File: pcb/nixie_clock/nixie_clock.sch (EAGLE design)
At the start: 38 parts, among them Q1 IRLR3110ZPBF, T1 DA2032-AL, U1 ESP32, U2 CP2102N, U3 LT3757

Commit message: sch and pcb outline
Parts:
- added C12: 0.22F, Passive Components > Capacitors > Supercapacitors \ Ultracapacitors:DSK-614/621
- added C13, C14, C18, C19: 1u, Passive Components > Capacitors > Multilayer Ceramic Capacitors MLCC:MLCC0603
- added C15: 22n, Passive Components > Capacitors > Multilayer Ceramic Capacitors MLCC:MLCC0603
- added C16, C17, C20, C23, C26, C27, C28, C29, C30, C31, C40: 100n, Passive Components > Capacitors > Multilayer Ceramic Capacitors MLCC:MLCC0603
- added C21: 4u7, Passive Components > Capacitors > Multilayer Ceramic Capacitors MLCC:MLCC0603
- added C22: 100p, Passive Components > Capacitors > Multilayer Ceramic Capacitors MLCC:MLCC0603
- added C24, C25: 15p, Passive Components > Capacitors > Multilayer Ceramic Capacitors MLCC:MLCC0603
- added C32: 10n, Passive Components > Capacitors > Multilayer Ceramic Capacitors MLCC:MLCC0603
- added C33: 3n, Passive Components > Capacitors > Multilayer Ceramic Capacitors MLCC:MLCC0603
- added C34, C35: 270p, Passive Components > Capacitors > Multilayer Ceramic Capacitors MLCC:MLCC0603
- added C36, C37: 10p, Passive Components > Capacitors > Multilayer Ceramic Capacitors MLCC:MLCC0603
- added C38: 5p6, Passive Components > Capacitors > Multilayer Ceramic Capacitors MLCC:MLCC0603
- added C39: 2p4, Passive Components > Capacitors > Multilayer Ceramic Capacitors MLCC:MLCC0603
- added D6: B0530W, Semiconductors > Discrete Semiconductors > Diodes & Rectifiers > Schottky Diodes & Rectifiers:B0530W
- added D7, D8: LED0603, Opto-electronics > LED Emitters:LED0603
- added F1: (no value), Circuit Protection > Resettable Fuses - PPTC:PTC0805
- added J1: USB-C, Connectors > USB:USB-C
- added L1: 10u, Passive Components > Inductors, Chokes & Coils:INDUCTOR_NC_1210
- added L2: 2n7, Passive Components > Inductors, Chokes & Coils:INDUCTOR_NC_0603
- added NL1, NL2: NEON6X16, vacuum_tubes:NEON6X16
- added Q2, Q3, Q4, Q5, Q6, Q7: BC817-25, Semiconductors > Discrete Semiconductors > Transistors > Bipolar Transistors - BJT:BC817-25
- added R13: 94k, Passive Components > Resistors > Chip Resistors:RESISTOR0603
- added R14, R16, R25, R33, R34, R35: 10k, Passive Components > Resistors > Chip Resistors:RESISTOR0603
- added R15: 85k, Passive Components > Resistors > Chip Resistors:RESISTOR0603
- added R17, R18: 100k, Passive Components > Resistors > Chip Resistors:RESISTOR_1206
- added R23, R24, R28, R29: 11k5, Passive Components > Resistors > Chip Resistors:RESISTOR0603
- added R26: 47k5, Passive Components > Resistors > Chip Resistors:RESISTOR0603
- added R27: 22k1, Passive Components > Resistors > Chip Resistors:RESISTOR0603
- added R30, R31, R38: 1k, Passive Components > Resistors > Chip Resistors:RESISTOR0603
- added R32: 20k, Passive Components > Resistors > Chip Resistors:RESISTOR0603
- added R36, R37: 4k7, Passive Components > Resistors > Chip Resistors:RESISTOR0603
- added SW1, SW2: (no value), Eletromechanical > Switches > Tactile Switches:PUSH_BUTTON
- added U$1: MIC2619, Power > Switching Controllers:MIC2619
- added U4: DS3231, Semiconductors > Integrated Circuits - ICs > Clock & Timer ICs > Real Time Clock:DS3231
- added U5, U6: HV5522, Power > Power Switch:HV5522
- added U7: MCP1700T-3302TT, Power > LDO Voltage Regulators:MCP1700T-3302TT
- added U8: W25Q40BVSS, Semiconductors > Integrated Circuits - ICs > Memory ICs > Flash:W25Q40BVSS
- added X1: 32.768kHz, Passive Components > Frequency Control & Timing Devices > Crystals:CRYSTAL2-SMD-3215
- added X2: 26MHz, Passive Components > Frequency Control & Timing Devices > Crystals:CRYSTAL_4P
- R10, R11, R12, R9: value (none) -> 15k
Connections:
- new net !DSP_BL: U1.(DAC1/ADC2:8/RTC6)GPIO25
- new net !DSP_LE: U1.(GPIO15/ADC2:3/TOUCH3/RTC13/SPICSO/U0RTS)MTDO
- new net 12V: C14.P$1, C15.P$1, C16.P$1, C17.P$1, D6.C, R13.P$2, R15.P$2, U5.!POL, U5.VDD, U6.!POL, U6.VDD
- new net 3.3V: C19.P$1, C20.P$1, C21.P$1, C22.P$1, C23.P$1, C26.P$1, C27.P$1, C28.P$1, C30.P$1, C31.P$1, C40.P$1, R25.P$2, R28.P$2, R29.P$2, R35.P$2, R36.P$2, R37.P$2, R38.P$2, U1.VDD3P3_CPU, U1.VDD3P3_RTC, U1.VDDA, U1.VDDA3P3, U2.VDD@6, U2.VIO@5, U2.VREGIN@7, U4.VCC, U7.VO, U8.VCC
- new net CHIP_PU: Q3.C03, R28.P$1, SW1.LB, SW1.RB, U1.CHIP_PU
- new net DSP_BL_CLK: D2.CLKI@4, U1.(VSPICLK/HS1_DATA7)GPIO18
- new net DSP_BL_SDI: D2.SDI@3, U1.GPIO23
- new net DSP_CLK: U1.(GPIO14/ADC2:6/TOUCH6/RTC16/SPICLK)MTMS
- new net DSP_SDI: U1.(GPIO13/ADC2:4/TOUCH4/RTC14/SPID/U0CTS)MTCK
- new net DTR: Q2.EM2, R34.P$2, U2.DTR@23
- new net FLASH_SCK: U1.(GPIO6/SPICLK/HS1_CLK/U1CTS)SD_CLK, U8.CLK
- new net FLASH_SCS: U1.(GPIO11/SPICSO/HS1_CMD/U1RTS)SD_CMD, U8.!CS!
- new net FLASH_SDI: U1.(GPIO8/SPID/HS1_DATA1)SD_DATA1, U8.DI/IO0
- new net FLASH_SDO: U1.(GPIO7/SPI1/HS1_DATA0)SD_DATA0, U8.DO/IO1
- new net FLASH_SHD: U1.(GPIO9/SPIHD/HS1_DATA2/U1RX)SD_DATA2, U8.!HOLD!/IO3
- new net FLASH_SWP: U1.(GPIO10/SPIWP/HS1_DATA3/U1TX)SD_DATA3, U8.!WP!/IO2
- new net FLASH_VDD: C29.P$1, U1.VDD3P3_SDIO
- new net GPIO0-BOOT: Q2.C03, R29.P$1, SW2.LB, SW2.RB, U1.(ADC2:1/TOUCH1/RTC11/CLK_OUT1)GPIO0
- new net HFXTAL_N: C36.P$1, U1.XTAL_N, X2.1
- new net HFXTAL_P: C37.P$1, U1.XTAL_P, X2.2
- new net LED: D7.AN, U1.(VSPICS0/HS1_DATA6)GPIO5
- new net LFXTAL_N: C25.P$1, U1.32K_XN(GPIO33/ADC1:5/TOUCH8/RTC8), X1.2
- new net LFXTAL_P: C24.P$1, U1.32K_XP(GPIO32/ADC1:4/TOUCH9/RTC9), X1.1
- new net N$16: D6.A, L1.P$2, U$1.SW
- new net N$17: R13.P$1, R14.P$2, U$1.OVP
- new net N$18: C15.P$2, R15.P$1, R16.P$2, U$1.FB
- new net N$19: NL1.2, R17.P$1
- new net N$20: NL2.2, R18.P$1
- new net N$23: U5.SDO, U6.SDI
- new net N$72: D3.SDO@1, D4.SDI@3
- new net N$73: D3.CLKO@6, D4.CLKI@4
- new net N$74: F1.2, J1.VBUS@A4,A9,B9,B4
- new net N$75: J1.CC2@B5, R23.P$2
- new net N$76: D4.CLKO@6, D5.CLKI@4
- new net N$77: D4.SDO@1, D5.SDI@3
- new net N$78: J1.CC1@A5, R24.P$2
- new net N$79: R25.P$1, U2.RSTB@9
- new net N$80: D8.CA, R30.P$2
- new net N$81: D2.CLKO@6, D3.CLKI@4
- new net N$82: D2.SDO@1, D3.SDI@3
- new net N$83: R26.P$2, R27.P$1, U2.VBUS@8
- new net N$84: D7.CA, R31.P$2
- new net N$85: C33.P$1, R32.P$2, U1.CAP2
- new net N$86: C34.P$1, U1.SENSOR_VN(GPI39/ADC1:3/RTC3)
- new net N$87: C32.P$1, C33.P$2, R32.P$1, U1.CAP1
- new net N$88: C35.P$1, U1.SENSOR_VP(GPI36/ADC1:0/RTC0)
- new net N$89: C34.P$2, U1.SENSOR_CAPN(GPI38/ADC1:2/RTC2)
- new net N$90: C35.P$2, U1.SENSOR_CAPP(GPI37/ADC1:1/RTC1)
- new net N$91: C38.P$1, L2.P$2, U1.LNA_IN
- new net N$92: Q2.BA1, R33.P$1
- new net N$93: Q3.BA1, R34.P$1
- new net N$94: C38.P$2, C39.P$1, E1.SIGNAL
- new net N$95: C12.AN, U4.VBAT
- new net N$96: R35.P$1, U4.!RST
- new net NT1-0: NT1.0, U5.HVOUT11
- new net NT1-1: NT1.1, U5.HVOUT12
- new net NT1-2: NT1.2, U5.HVOUT13
- new net NT1-3: NT1.3, U5.HVOUT14
- new net NT1-4: NT1.4, U5.HVOUT15
- new net NT1-5: NT1.5, U5.HVOUT16
- new net NT1-6: NT1.6, U5.HVOUT17
- new net NT1-7: NT1.7, U5.HVOUT18
- new net NT1-8: NT1.8, U5.HVOUT19
- new net NT1-9: NT1.9, U5.HVOUT20
- new net NT2-0: NT2.0, U5.HVOUT1
- new net NT2-1: NT2.1, U5.HVOUT2
- new net NT2-2: NT2.2, U5.HVOUT3
- new net NT2-3: NT2.3, U5.HVOUT4
- new net NT2-4: NT2.4, U5.HVOUT5
- new net NT2-5: NT2.5, U5.HVOUT6
- new net NT2-6: NT2.6, U5.HVOUT7
- new net NT2-7: NT2.7, U5.HVOUT8
- new net NT2-8: NT2.8, U5.HVOUT9
- new net NT2-9: NT2.9, U5.HVOUT10
- new net RTC_INT: R38.P$1, U1.(ADC2:0/TOUCH0/RTC10/SPIHD)GPIO4, U4.!INT!/SQW
- new net RTS: Q3.EM2, R33.P$2, U2.RTS@19
- new net SCL: R37.P$1, U1.(VSPIWP/HS2_CLK)GPIO22, U4.SCL
- new net SDA: R36.P$1, U1.(VSPIHD/HS2_CMD)GPIO21, U4.SDA
- new net U0RXD: U1.(GPIO3/CLK_OUT2/HS2_DATA0)U0RXD, U2.TXD@21
- new net U0TXD: U1.(GPIO1/CLK_OUT3/HS2_DATA1)U0TXD, U2.RXD@20
- new net USB_DM: J1.DN@A7,B7, U2.D-@4
- new net USB_DP: J1.DP@A6,B6, U2.D+@3
- net !HVEN: now also U1.(DAC2/ADC2:9/RTC7)GPIO26
- net 5V: now also C13.P$1, C18.P$1, D2.VDD@5, D3.VDD@5, D4.VDD@5, D5.VDD@5, D8.AN, F1.1, L1.P$1, R27.P$2, U$1.EN, U$1.VIN, U7.VI
- net GND: now also C12.CA, C13.P$2, C14.P$2, C16.P$2, C17.P$2, C18.P$2, C19.P$2, C20.P$2, C21.P$2, C22.P$2, C23.P$2, C24.P$2, C25.P$2, C26.P$2, C27.P$2, C28.P$2, C29.P$2, C30.P$2, C31.P$2, C32.P$2, C36.P$2, C37.P$2, C39.P$2, C40.P$2, D2.GND@2, D3.GND@2, D4.GND@2, D5.GND@2, E1.GND, J1.GND@A1,A12,B12,B1, J1.SHIELD, L2.P$1, R14.P$1, R16.P$1, R23.P$1, R24.P$1, R26.P$1, R30.P$1, R31.P$1, SW1.LT, SW1.RT, SW2.LT, SW2.RT, U$1.GND, U1.GND, U2.GND@2, U2.GND@PAD, U4.GND, U4.NC, U5.GND, U6.GND, U7.GND, U8.GND, X2.GND@0, X2.GND@1
- net VOUT: now also R17.P$2, R18.P$2
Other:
- note added: "32.768kHz RTC Crystal"
- note added: "Auto-Reset"
- note added: "Boot Mode Configuration Pin Default Boot Download GPIO0 1 1 0 U0TXD 1 1 x GPIO2 0 x 0 GPIO4 0 x x MTDO 1 x x GPIO5 1 1 x If U0TXD, GPIO2, GPIO5 are floating, GPIO0 determines boot mode"
- note added: "CHIP_PU is the ESP32's enable/reset pin. It must be pulled high to turn the ESP32 on."
- note added: "CP2102N (USB-to-Serial Converter)"
- note added: "DS3231 RTCC"
- note added: "Espressif ESP32"
- note added: "GPIO0 Button"
- note added: "GPIO5 LED"
- note added: "Headers"
- note added: "If DTR is LOW, toggling RTS from HIGH to LOW resets to run mode. If RTS is HIGH, toggling DTR from LOW to HIGH resets to bootloader."
- note added: "Near VDDA 46, 43"
- note added: "Near VDDA3P3 3, 4"
- note added: "Near VDDA_LNA 1"
- note added: "Near VDDPST_CPU 37"
- note added: "Near VDDPST_RTC 19"
- note added: "Near VDDPST_SDIO 26"
- note added: "R13: 10k R14: 85K Vo: 12.017 V"
- note added: "R13: 10k R14: 94k OVP: 13.156 V"
- note added: "Reset Button"
- note added: "SJ3 allows selection between FLASH_VDD and 3.3V as the voltage supply to the flash IC."
- note added: "Vfb = 1.265 V"
- note added: "Voltage Regulator and input connector"
- note added: "W25Q32FVSS - 4MB SPI Flash"
- moved on the sheet: D2, D3, D4, D5, E1, NT1, NT2, NT3, NT4, R10, R11, R12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

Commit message: rough pcb done
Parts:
- removed U$1: MIC2619, Power > Switching Controllers:MIC2619
- added C41, C42, C43, C44: (no value), Passive Components > Capacitors > Multilayer Ceramic Capacitors MLCC:MLCC0603
- added C45: 47u, Passive Components > Capacitors > Multilayer Ceramic Capacitors MLCC:MLCC_1210
- added D9: BAT54S, Semiconductors > Discrete Semiconductors > Diodes & Rectifiers > Schottky Diodes & Rectifiers:BAT54S
- added J2, J3: 8, Connectors > Header:8
- added J4, J5: 4, Connectors > Header:4
- added LOGO1, LOGO8: DESIGNEDINPT, Utility > Silkscreen:DESIGNEDINPT
- added LOGO2: RAFAEL_SILVA10CIRCLE, Utility > Silkscreen:RAFAEL_SILVA10CIRCLE
- added LOGO3, LOGO9: OSHW-LOGOL, Utility > Silkscreen:OSHW-LOGOL
- added LOGO4, LOGO6: HV_WARNING, Silkscreen:HV_WARNING
- added LOGO5: RADIO-10MM, Silkscreen:RADIO-10MM
- added LOGO7: RAFAEL_SILVA10MM, Utility > Silkscreen:RAFAEL_SILVA10MM
- added R19, R21, R22, R39, R40, R41, R42: 1k, Passive Components > Resistors > Chip Resistors:RESISTOR0603
- added R20: 94k, Passive Components > Resistors > Chip Resistors:RESISTOR0603
- added R43: 100, Passive Components > Resistors > Chip Resistors:RESISTOR0603
- added R44: 10k, Passive Components > Resistors > Chip Resistors:RESISTOR0603
- added U10, U11: 74LVC1G17, Semiconductors > Integrated Circuits - ICs > Logic ICs > Logic Gates:74LVC1G17
- added U9: MIC2619, Power > Switching Controllers:MIC2619
- C33: value 3n -> 3n3
- E1: value ANTENNATRACE-15.2MM -> ANTENNATRACE; device Passive Components > Antennas:ANTENNATRACE-15.2MM -> Passive Components > Antennas:ANTENNATRACE
- R6: value 10k -> 100k
- R7: value 75k -> 10k
- SW1, SW2: device Eletromechanical > Switches > Tactile Switches:PUSH_BUTTON -> Eletromechanical > Switches > Tactile Switches:PUSH_BUTTON3X4X2
- U7: value MCP1700T-3302TT -> MIC39100; device Power > LDO Voltage Regulators:MCP1700T-3302TT -> Power > LDO Voltage Regulators:MIC39100
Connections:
- removed net N$94: C38.P$2, C39.P$1, E1.SIGNAL
- new net !DSP_BL_HL: J2-7.S, Q7.C03, R42.P$1
- new net !DSP_LE_HL: J2-6.S, Q6.C03, R41.P$1
- new net BR2_DSP_CLK_HL: J3-5.S, U5.CLK, U6.CLK
- new net BRD2_!DSP_BL_HL: J3-7.S, U5.!BL, U6.!BL
- new net BRD2_!DSP_LE_HL: J3-6.S, U5.!LE, U6.!LE
- new net BRD2_12V: C16.P$1, C17.P$1, J3-3.S, U5.!POL, U5.VDD, U6.!POL, U6.VDD
- new net BRD2_GND2: C16.P$2, C17.P$2, J3-8.S, U5.GND, U6.GND
- new net BRD2_SDP_SDI_HL: J3-4.S, U5.SDI
- new net BRD2_VOUT: J3-1.S, R10.P$2, R11.P$2, R12.P$2, R17.P$2, R18.P$2, R9.P$2
- new net DSP_CLK_HL: J2-5.S, Q5.C03, R40.P$1
- new net LED_GND: C41.P$2, C42.P$2, C43.P$2, C44.P$2, D2.GND@2, D3.GND@2, D4.GND@2, D5.GND@2, J5-2.S
- new net LED_VCC: C41.P$1, C42.P$1, C43.P$1, C44.P$1, D2.VDD@5, D3.VDD@5, D4.VDD@5, D5.VDD@5, J5-3.S
- new net N$21: Q4.BA1, R19.P$2
- new net N$22: Q5.BA1, R20.P$2
- new net N$24: Q7.BA1, R22.P$2
- new net N$25: Q6.BA1, R21.P$2
- new net N$26: D2.SDI@3, J5-1.S
- new net N$27: D2.CLKI@4, J5-4.S
- new net N$28: C39.P$1, E1.SIGNAL, L2.P$1
- new net N$29: J4-4.S, U11.1.Y
- new net N$30: J4-1.S, U10.1.Y
- new net N$31: D9.3, R43.P$2
- new net N$32: R44.P$2, R6.3, U3.FB
- new net NL1: NL1.2, U6.HVOUT21
- new net NL2: NL2.2, U6.HVOUT22
- new net NT3-0: NT3.0, U6.HVOUT11
- new net NT3-1: NT3.1, U6.HVOUT12
- new net NT3-2: NT3.2, U6.HVOUT13
- new net NT3-3: NT3.3, U6.HVOUT14
- new net NT3-4: NT3.4, U6.HVOUT15
- new net NT3-5: NT3.5, U6.HVOUT16
- new net NT3-6: NT3.6, U6.HVOUT17
- new net NT3-7: NT3.7, U6.HVOUT18
- new net NT3-8: NT3.8, U6.HVOUT19
- new net NT3-9: NT3.9, U6.HVOUT20
- new net NT4-0: NT4.0, U6.HVOUT1
- new net NT4-1: NT4.1, U6.HVOUT2
- new net NT4-2: NT4.2, U6.HVOUT3
- new net NT4-3: NT4.3, U6.HVOUT4
- new net NT4-4: NT4.4, U6.HVOUT5
- new net NT4-5: NT4.5, U6.HVOUT6
- new net NT4-6: NT4.6, U6.HVOUT7
- new net NT4-7: NT4.7, U6.HVOUT8
- new net NT4-8: NT4.8, U6.HVOUT9
- new net NT4-9: NT4.9, U6.HVOUT10
- new net SDP_SDI_HL: J2-4.S, Q4.C03, R39.P$1
- net !DSP_BL: now also R22.P$1
- net !DSP_LE: now also R21.P$1
- net 12V: now also J2-3.S, R39.P$2, R40.P$2, R41.P$2, R42.P$2; no longer C16.P$1, C17.P$1, U5.!POL, U5.VDD, U6.!POL, U6.VDD
- net 3.3V: now also D9.1, U7.VOUT; no longer U7.VO
- net 5V: now also C45.P$1, J4-3.S, U10.PW.VCC, U11.PW.VCC, U7.VIN, U9.EN, U9.VIN; no longer D2.VDD@5, D3.VDD@5, D4.VDD@5, D5.VDD@5, U$1.EN, U$1.VIN, U7.VI
- net CHIP_PU: now also SW1.4; no longer SW1.LB, SW1.RB
- net DSP_BL_CLK: now also U11.1.A; no longer D2.CLKI@4
- net DSP_BL_SDI: now also U10.1.A; no longer D2.SDI@3
- net DSP_CLK: now also R20.P$1
- net DSP_SDI: now also R19.P$1
- net GND: now also C38.P$2, C45.P$2, J2-8.S, J4-2.S, Q4.EM2, Q5.EM2, Q6.EM2, Q7.EM2, R44.P$1, SW1.1, SW1.2, SW2.1, SW2.2, T1.1, U10.PW.GND, U11.PW.GND, U7.GND_(TAB), U7.GND_(TAB)_2, U9.GND; no longer C16.P$2, C17.P$2, D2.GND@2, D3.GND@2, D4.GND@2, D5.GND@2, L2.P$1, R6.2, SW1.LT, SW1.RT, SW2.LT, SW2.RT, U$1.GND, U5.GND, U6.GND, U7.GND
- net GPIO0-BOOT: now also SW2.4; no longer SW2.LB, SW2.RB
- net HFXTAL_N: now also C37.P$1, X2.2; no longer C36.P$1, X2.1
- net HFXTAL_P: now also C36.P$1, X2.1; no longer C37.P$1, X2.2
- net N$16: now also U9.SW; no longer U$1.SW
- net N$17: now also U9.OVP; no longer U$1.OVP
- net N$18: now also U9.FB; no longer U$1.FB
- net N$19: now also NL1.1; no longer NL1.2
- net N$20: now also NL2.1; no longer NL2.2
- net N$8: now also R6.2; no longer R6.1, U3.FB
- net N$95: now also R43.P$1
- net VOUT: now also J2-1.S; no longer R10.P$2, R11.P$2, R12.P$2, R17.P$2, R18.P$2, R9.P$2
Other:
- note added: "To nixie board -->"

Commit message: rough pcb done
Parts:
- removed LOGO1: DESIGNEDINPT, Utility > Silkscreen:DESIGNEDINPT
- removed LOGO2: RAFAEL_SILVA10CIRCLE, Utility > Silkscreen:RAFAEL_SILVA10CIRCLE
- removed LOGO4: HV_WARNING, Silkscreen:HV_WARNING
- removed LOGO5: RADIO-10MM, Silkscreen:RADIO-10MM
- removed LOGO7: RAFAEL_SILVA10MM, Utility > Silkscreen:RAFAEL_SILVA10MM
- removed LOGO9: OSHW-LOGOL, Utility > Silkscreen:OSHW-LOGOL
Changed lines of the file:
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@@
 <part name="C45" library="Passive Components &gt; Capacitors &gt; Multilayer Ceramic Capacitors MLCC" deviceset="MLCC" device="_1210" value="47u"/>
 <part name="GND26" library="Utility &gt; Power Symbols" deviceset="GND" device=""/>
-<part name="LOGO1" library="Utility &gt; Silkscreen" deviceset="DESIGNEDINPT" device=""/>
-<part name="LOGO2" library="Utility &gt; Silkscreen" deviceset="RAFAEL_SILVA" device="10CIRCLE"/>
 <part name="LOGO3" library="Utility &gt; Silkscreen" deviceset="OSHW-LOGO" device="L"/>
-<part name="LOGO4" library="Silkscreen" deviceset="HV_WARNING" device=""/>
-<part name="LOGO5" library="Silkscreen" deviceset="RADIO" device="-10MM"/>
 <part name="LOGO6" library="Silkscreen" deviceset="HV_WARNING" device=""/>
-<part name="LOGO7" library="Utility &gt; Silkscreen" deviceset="RAFAEL_SILVA" device="10MM"/>
 <part name="LOGO8" library="Utility &gt; Silkscreen" deviceset="DESIGNEDINPT" device=""/>
-<part name="LOGO9" library="Utility &gt; Silkscreen" deviceset="OSHW-LOGO" device="L"/>
 </parts>
 <sheets>
@@
 <attribute name="VALUE" x="177.8" y="197.866" size="1.778" layer="96" align="top-center"/>
 </instance>
-<instance part="LOGO1" gate="G$1" x="281.94" y="38.1" smashed="yes"/>
-<instance part="LOGO2" gate="G$1" x="302.26" y="40.64" smashed="yes"/>
 <instance part="LOGO3" gate="G$1" x="327.66" y="48.26" smashed="yes"/>
-<instance part="LOGO4" gate="G$1" x="353.06" y="45.72" smashed="yes"/>
-<instance part="LOGO5" gate="G$1" x="363.22" y="40.64" smashed="yes"/>
 <instance part="LOGO6" gate="G$1" x="353.06" y="55.88" smashed="yes"/>
-<instance part="LOGO7" gate="G$1" x="302.26" y="50.8" smashed="yes"/>
 <instance part="LOGO8" gate="G$1" x="299.72" y="55.88" smashed="yes"/>
-<instance part="LOGO9" gate="G$1" x="337.82" y="71.12" smashed="yes"/>
 </instances>
 <busses>

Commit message: finished board -TODO change usb connector
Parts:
- removed LOGO8: DESIGNEDINPT, Utility > Silkscreen:DESIGNEDINPT
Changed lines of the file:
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@@
 <part name="LOGO3" library="Utility &gt; Silkscreen" deviceset="OSHW-LOGO" device="L"/>
 <part name="LOGO6" library="Silkscreen" deviceset="HV_WARNING" device=""/>
-<part name="LOGO8" library="Utility &gt; Silkscreen" deviceset="DESIGNEDINPT" device=""/>
 </parts>
 <sheets>
@@
 <instance part="LOGO3" gate="G$1" x="327.66" y="48.26" smashed="yes"/>
 <instance part="LOGO6" gate="G$1" x="353.06" y="55.88" smashed="yes"/>
-<instance part="LOGO8" gate="G$1" x="299.72" y="55.88" smashed="yes"/>
 </instances>
 <busses>

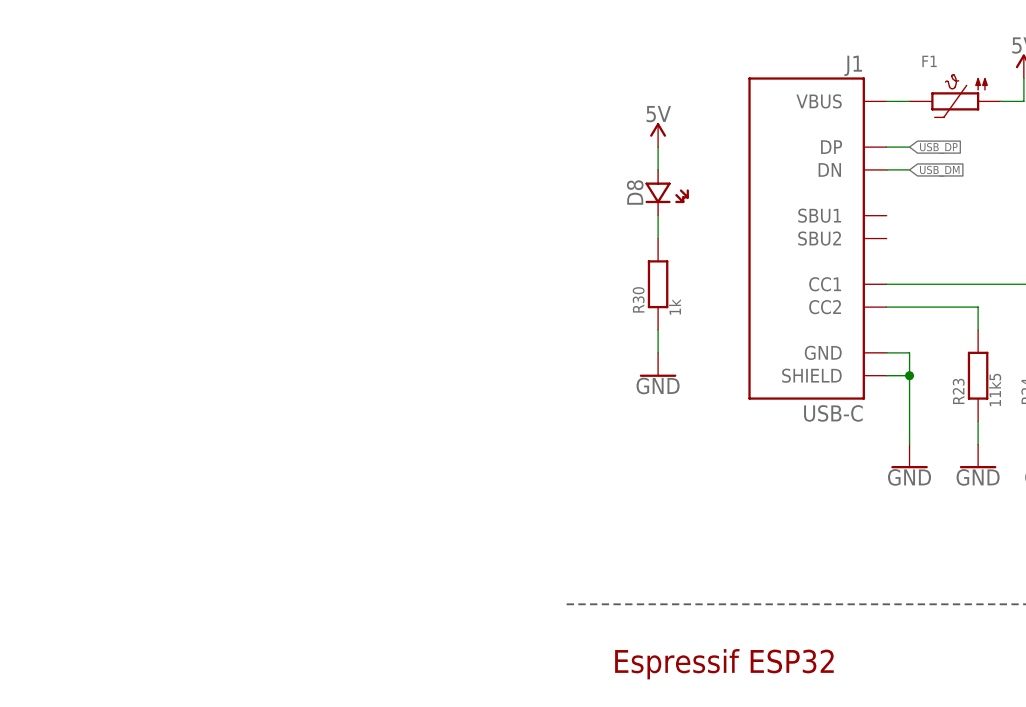
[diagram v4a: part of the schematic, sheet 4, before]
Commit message: changed usb connector
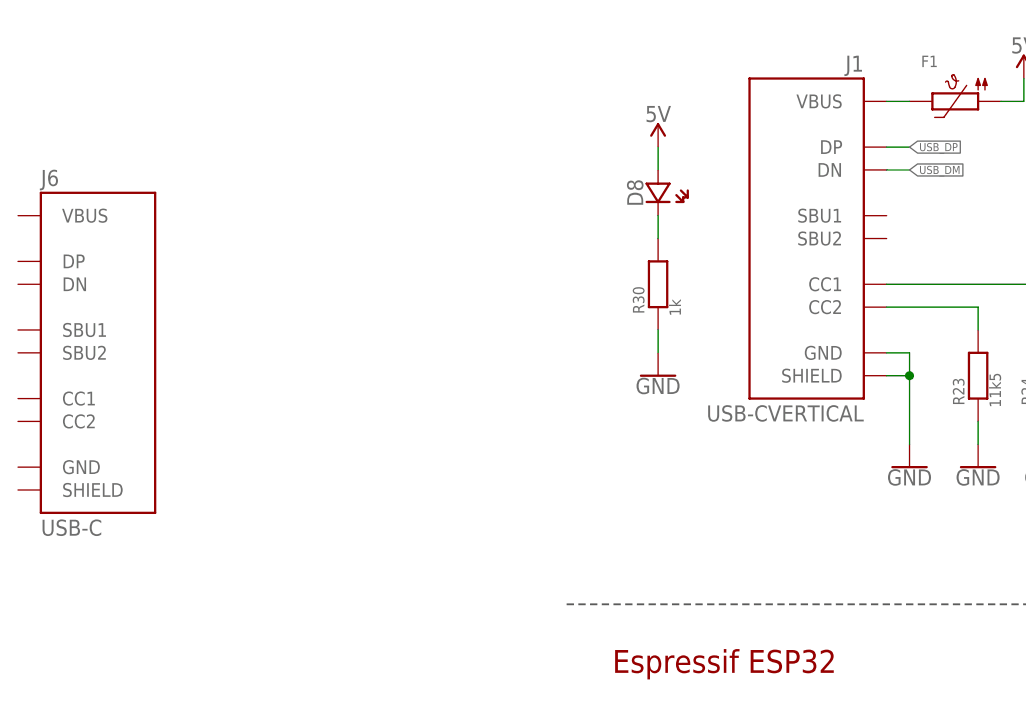
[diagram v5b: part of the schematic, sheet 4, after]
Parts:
- added J6: USB-C, Connectors > USB:USB-C
- J1: value USB-C -> USB-CVERTICAL; device Connectors > USB:USB-C -> Connectors > USB:USB-CVERTICAL
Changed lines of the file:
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@@
 <part name="SUPPLY18" library="Utility &gt; Power Symbols" deviceset="5V" device=""/>
 <part name="SUPPLY19" library="Utility &gt; Power Symbols" deviceset="3.3V" device=""/>
-<part name="J1" library="Connectors &gt; USB" deviceset="USB-C" device=""/>
+<part name="J1" library="Connectors &gt; USB" deviceset="USB-C" device="VERTICAL" value="USB-CVERTICAL"/>
 <part name="F1" library="Circuit Protection &gt; Resettable Fuses - PPTC" deviceset="PTC" device="0805"/>
 <part name="SUPPLY20" library="Utility &gt; Power Symbols" deviceset="5V" device=""/>
@@
 <part name="LOGO3" library="Utility &gt; Silkscreen" deviceset="OSHW-LOGO" device="L"/>
 <part name="LOGO6" library="Silkscreen" deviceset="HV_WARNING" device=""/>
+<part name="J6" library="Connectors &gt; USB" deviceset="USB-C" device=""/>
 </parts>
 <sheets>
@@
 <attribute name="VALUE" x="76.2" y="200.406" size="1.778" layer="96" align="top-center"/>
 </instance>
+<instance part="J6" gate="G$1" x="-58.42" y="180.34" smashed="yes">
+<attribute name="VALUE" x="-58.42" y="177.8" size="1.778" layer="96"/>
+<attribute name="NAME" x="-58.42" y="218.44" size="1.778" layer="95" align="top-left"/>
+</instance>
 </instances>

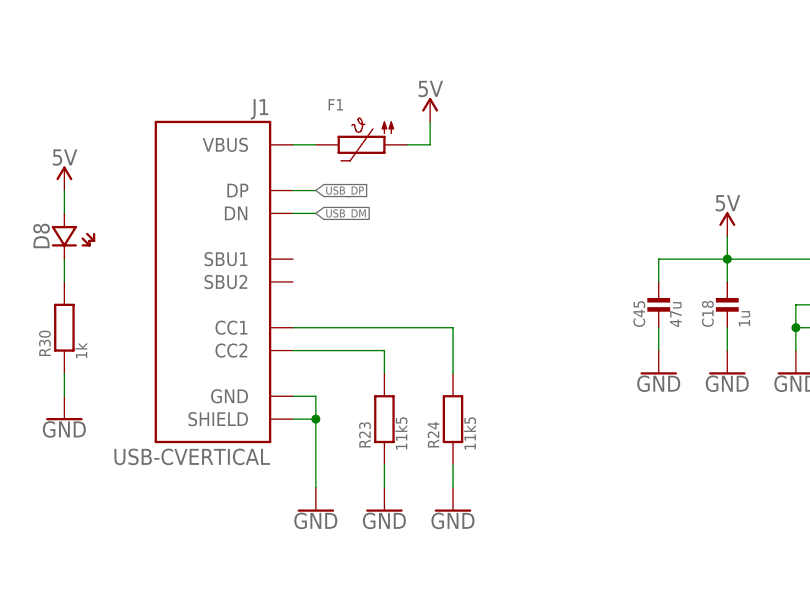
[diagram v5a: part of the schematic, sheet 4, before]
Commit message: corrected usb pd resistor values
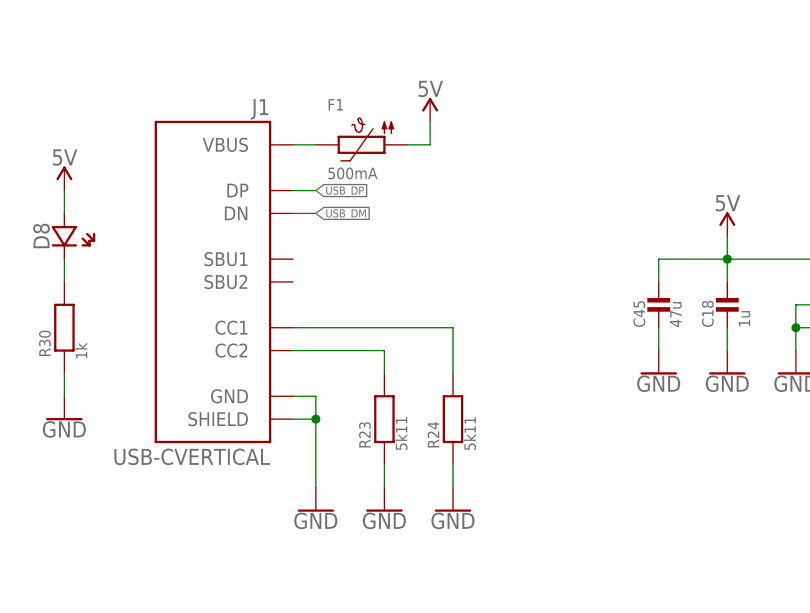
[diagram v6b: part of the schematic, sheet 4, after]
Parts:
- F1: value (none) -> 500mA
- R23, R24: value 11k5 -> 5k11
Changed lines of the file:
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@@
 <?xml version="1.0" encoding="utf-8"?>
 <!DOCTYPE eagle SYSTEM "eagle.dtd">
-<eagle version="9.5.2">
+<eagle version="9.5.1">
 <drawing>
 <settings>
@@
 <part name="SUPPLY19" library="Utility &gt; Power Symbols" deviceset="3.3V" device=""/>
 <part name="J1" library="Connectors &gt; USB" deviceset="USB-C" device="VERTICAL" value="USB-CVERTICAL"/>
-<part name="F1" library="Circuit Protection &gt; Resettable Fuses - PPTC" deviceset="PTC" device="0805"/>
+<part name="F1" library="Circuit Protection &gt; Resettable Fuses - PPTC" deviceset="PTC" device="0805" value="500mA"/>
 <part name="SUPPLY20" library="Utility &gt; Power Symbols" deviceset="5V" device=""/>
 <part name="GND28" library="Utility &gt; Power Symbols" deviceset="GND" device=""/>
-<part name="R23" library="Passive Components &gt; Resistors &gt; Chip Resistors" deviceset="RESISTOR" device="0603" value="11k5"/>
-<part name="R24" library="Passive Components &gt; Resistors &gt; Chip Resistors" deviceset="RESISTOR" device="0603" value="11k5"/>
+<part name="R23" library="Passive Components &gt; Resistors &gt; Chip Resistors" deviceset="RESISTOR" device="0603" value="5k11"/>
+<part name="R24" library="Passive Components &gt; Resistors &gt; Chip Resistors" deviceset="RESISTOR" device="0603" value="5k11"/>
 <part name="GND29" library="Utility &gt; Power Symbols" deviceset="GND" device=""/>
 <part name="GND30" library="Utility &gt; Power Symbols" deviceset="GND" device=""/>
